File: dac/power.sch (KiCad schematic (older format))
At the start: 30 parts, among them Q2 2STD1665T4, U4 OPA830

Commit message: More work on dac/power.sch and dac/reference_buffer.sch. Also, fixed comments in input/reference_buffer.sch
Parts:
- removed C39: 1uF, Capacitor_SMD:C_0805_2012Metric, symbol Device:C_Small
- removed C7: 330uF, Capacitor_SMD:CP_Elec_8x6.7, symbol Device:CP1_Small
- removed D15: 5V (standoff), Diode_SMD:D_SMA, symbol Device:D_Zener
- removed F?: 750 mA 90 mOhm, Fuse:Fuse_1206_3216Metric, symbol Device:Polyfuse
- removed R19, R?: 180, Resistor_SMD:R_0805_2012Metric, symbol Device:R_US
- removed U4: OPA830, Package_SO:SOIC-8_3.9x4.9mm_P1.27mm, symbol ilemt_input:opamp_single
- added C11, C23, C24: 10uF, Capacitor_SMD:C_0603_1608Metric, symbol Device:C_Small
- added C21, C22: 1uF, Capacitor_SMD:C_0805_2012Metric, symbol Device:C_Small
- added C25, C26: 330uF, Capacitor_SMD:CP_Elec_8x6.7, symbol Device:CP1_Small
- added D4: 5V (standoff), Diode_SMD:D_SMA, symbol Device:D_Zener
- added FB4: 21 Ohm, Inductor_SMD:L_0805_2012Metric, symbol dk_Ferrite-Beads-and-Chips:MPZ2012S601AT000
- added J1: Aux power, digikey-footprints:PinHeader_1x3_P2.54_Drill1.1mm, symbol dk_Rectangular-Connectors-Headers-Male-Pins.lib:640456-3
- added R10, R9: 0, Resistor_SMD:R_0603_1608Metric, symbol Device:R_US
- added R12, R16, R17, R18: 200, Resistor_SMD:R_0603_1608Metric, symbol Device:R_US
- added R13, R14: 1K, Resistor_SMD:R_0603_1608Metric, symbol Device:R_US
- added TP4: +8V, TestPoint:TestPoint_THTPad_D1.5mm_Drill0.7mm, symbol Connector:TestPoint
- added TP5: -12V, TestPoint:TestPoint_THTPad_D1.5mm_Drill0.7mm, symbol Connector:TestPoint
- added U3: OP27, Package_SO:SOIC-8_3.9x4.9mm_P1.27mm, symbol ilemt_input:opamp_single
- added U5: NCP1117STAT3G, Package_TO_SOT_SMD:SOT-223, symbol dk_PMIC-Voltage-Regulators-Linear:NCP1117ST33T3G
- added U6: LM337_SOT223, Package_TO_SOT_SMD:SOT-223-3_TabPin2, symbol Regulator_Linear:LM337_SOT223
- C12: value 47pF -> 220pF
- D8: value 10V (standoff) -> 15V (standoff); DK line 41 -> (none); Description TVS DIODE 10V 17V DO214AC -> (none); Digikey 732-9947-1-ND -> (none); MPN 824500500 -> (none); Manufacturer Würth Elektronik -> (none)
- R15: value 10 -> 1.74K; footprint Resistor_SMD:R_0805_2012Metric -> Resistor_SMD:R_0603_1608Metric; DK line 9 -> (none); Description RES SMD 10 OHM 5% 1/2W 0805 -> (none); Digikey 541-10TACT-ND -> (none); MPN CRCW080510R0JNEAHP -> (none); Manufacturer Vishay Dale -> (none); Notes Thick film surge resist -> (none)
- R17: value 33 -> 10
- gave numbers to parts that had none: 2
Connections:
- net labels added: U8IN, VDD
- net labels removed: FILT_+10V, FILT_-6V, OVDD, Q2E, U4+, U4-, U4OUT, U4V+, U4V-
- wire segments 99 -> 147
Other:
- note added: "Analog supplies\nV+ : +8V (200 mA max)\nV- : -12V (100 mA max)"
- note added: "C11/R13 is a low-effort 16 Hz lowpass\nto suppress HF crud that may come in on\nthe master VREF so that it does not go\ninto VCC."
- note added: "C20 ESR is critical for stability. It acts as a subber to\nstabilize the interaction with low-ESR ceramic \nbypass caps. This is an aluminum solid polymer type, \nchosen to have ESR near 25 mOhm.\nIf the ESR is too low it will be destabilizing.\n\nD4 prevents VCC from floating up\nif current is sourced into VCC,\nor on startup."
- note added: "DAC analog supply\nVCC : +5V (80 mA max)"
- note added: "DAC digital supply\nVDD : +3.3V (100 mA max, 25 mA typ)"
- note added: "FB4 and R10 prevent open-loop\nHF parastitic instability in Q1, when\nlooking into the capacitive load. \n\nOn an output short, current limiting\nis imposed by dragging down V+,\nwhich is current limited by U5."
- note added: "R12 prevents U3 from having to source current\nnear its positive rail. Instead it is always sinking,\na nominal current of 8 mA."
- note added: "Remote sense at bus"
- note added: "These supplies are mainly for the output opamps, but the\nnoise-critical DAC analog VCC supply is drawn from V+ also."
- note added: "VCC is noise critical because the DAC reference\nis with respect to VCC. Any 1/f noise in VCC will\nshow up on the ADC reference. See reference_buffer."
- note added: "We need a more negative supply than -6V, so that will\ncome in here from somewhere else."
- note removed: "### use opamp with low 1/f noise, doesn't really need all that bandwidth\nAny 1/f noise in VCC is going to appear in the VCOM DAC reference."
- note removed: "+3.3V digital"
- note removed: "D15, D16 prevent V+/V- from floating up\nif current is sourced into the rails, such as\nfrom the sensor input via the clamp diodes."
- note removed: "Note: \nF1, F2 fuse resistance is part of loop compensation.\nIf resistance is far from 100 mOhm this affects bandwidth \nand stability. This part has a low spread between pre-trip\nand post-trip resistance Resistance was the primary selection\ncriterion. Getting a low enough resistance forces a \nsomewhat high trip current. \n\nC14, C15 ESR is critical for stability. This is an aluminum\nsolid p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"
- note removed: "R15/C7 and R16/C11 boost the 10 kHz supply rejection\nabove the U5, U6 PSRR (which will be low in a high speed type)"
- note removed: "Remote sense at bus tap"
- note removed: "These regulators for the V+, V- analog supplies operate at a lowish dropout of about 1.5V\nand clean up any crud on the incoming supplies. They also give a supply referenced\nto the local ground which is extremely stiff at our operating frequency near 10 kHz.\nThis prevents coupling between channels via the supply. \n\nThe outputs are derived from the VREF 5V reference, which has to be low noise,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"
- note removed: "VCC regulator, +5V"
- moved on the sheet: C12, C14, C15, C16, C18, C19, C20, C27, D2, D3, FB2, FB3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

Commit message: Much progress on the DAC card.  Schematic is complete, starting on placement.
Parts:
- removed C11, C23, C24: 10uF, Capacitor_SMD:C_0603_1608Metric, symbol Device:C_Small
- removed C20, C21, C25, C26: 330uF, Capacitor_SMD:CP_Elec_8x6.7, symbol Device:CP1_Small
- removed C32: 10nF, Capacitor_SMD:C_0805_2012Metric, symbol Device:C_Small
- removed D4: 10V (standoff), Diode_SMD:D_SMA, symbol Device:D_Zener
- added C15, C16, C22, C23: 47uF, Capacitor_SMD:CP_Elec_6.3x7.7, symbol Device:CP1_Small
- added C20, C21, C8: 10uF 16V, Capacitor_SMD:C_0805_2012Metric, symbol Device:C_Small
- added D2, D5, D6: 15V (standoff), Diode_SMD:D_SMA, symbol Device:D_Zener
- C14: renamed from C12; Description 47pF ±5% 50V Ceramic Capacitor C0G, NP0 0603 (1608 Metric) -> (none); Digikey 311-1065-1-ND -> (none); MPN CC0603JRNPO9BN470 -> (none); Manufacturer Yageo -> (none)
- R16: renamed from R17; footprint Resistor_SMD:R_0603_1608Metric -> Resistor_SMD:R_0805_2012Metric; Description RES 33 OHM 1% 1/10W 0603 -> RES SMD 10 OHM 5% 1/2W 0805; Digikey RMCF0603FT33R0CT-ND -> 541-10TACT-ND; MPN RMCF0603FT33R0 -> CRCW080510R0JNEAHP; Manufacturer Stackpole Electronics Inc -> Vishay Dale; Notes (none) -> Thick film surge resist
- TP2: renamed from TP6; footprint TestPoint:TestPoint_THTPad_D1.5mm_Drill0.7mm -> TestPoint:TestPoint_Keystone_5000-5004_Miniature
- TP3: renamed from TP8; value +5V VCC -> +5V DAC_VCC; footprint TestPoint:TestPoint_THTPad_D1.5mm_Drill0.7mm -> TestPoint:TestPoint_Keystone_5000-5004_Miniature
- TP4, TP5: footprint TestPoint:TestPoint_THTPad_D1.5mm_Drill0.7mm -> TestPoint:TestPoint_Keystone_5000-5004_Miniature
- U3: value OP27 -> OPA1611; DK line 15 -> (none); Description IC OPAMP GP 1 CIRCUIT 8SOIC -> (none); Digikey 296-31706-1-ND -> (none); MPN OPA27GU/2K5 -> (none); Manufacturer Texas Instruments -> (none)
- renumbered C22 to C10, C16 to C11, C17 to C12, C25 to C13, C14 to C17, C21 to C18, C22 to C19, C8 to C9, D8 to D3, FB3 to FB1, FB1 to FB3, J1 to J5, Q2 to Q1, R9 to R14, R10 to R15, R12 to R17, R14 to R19, R15 to R20, R16 to R21, R17 to R22, TP4 to TP6
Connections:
- net VDD is gone; now on net VCC: C13.1, TP2.1, U4.3 (VO)
- net GND: now also C15.2, C16.1, C20.1, C21.1, C22.2, C23.1, C8.1, D2.2 (A)
- net V+: now also C22.1, D6.2 (A)
- net V-: now also C23.2, D5.1 (K)
- net VCC: no longer C17.1, D4.1 (K), FB4.2, R18.2, TP3.1
- net U3-: now reaches C14.1, R18.1, U3.2 (-)
- net Q1E: now reaches C14.2, FB4.1, Q1.3 (E)
- net Q1B: now reaches Q1.1 (B), R16.1, R17.2
- net V-_UNREG: now reaches C12.1, C19.2, D3.2 (A), FB3.2, U6.2 (VI)
- net V-_UNREG: now also C16.2, D5.2 (A)
- net V-_RAW: now reaches FB3.1, J5.3, R15.2
- net V+_RAW: now reaches FB2.1, J5.2, R14.2
- net V+_ADJ: now reaches R19.1, R21.1, U5.1 (ADJ/GND)
- net V+_ADJ: now also C20.2
- net V-_ADJ: now reaches R20.1, R22.1, U6.1 (ADJ)
- net V-_ADJ: now also C21.2
- net U3+: now reaches R13.1, U3.3 (+)
- net U3+: now also C8.2
- net RAW_+10V renamed +10V
- net RAW_+5VDIG renamed +5VDIG
- net RAW_-6V renamed -6V
- net U7IN renamed U4_IN
- net U8IN renamed V+_UNREG
- net V+_UNREG: now also C15.1, D2.1 (K), D6.1 (K)
- new net DAC_VCC: C17.1, D4.1 (K), FB4.2, R18.2, TP3.1
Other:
- note added: "Analog supplies\nV+ : +8V (200 mA max)\nV- : -12V (200 mA max)"
- note added: "C17 ESR is critical for stability. If the ESR is too low it\nwill be destabilizing. It acts as a snubber to stabilize\nthe interaction with low-ESR ceramic bypass caps. This is\nan aluminum solid polymer type, chosen to have ESR near 25\nmOhm.\n\nD4 prevents VCC from floating up if current is sourced into\nVCC, or on startup."
- note added: "C8/R13 is a low-effort 16 Hz lowpass\nto suppress HF crud that may come in on\nthe master VREF so that it does not go\ninto DAC_VCC."
- note added: "D5, D6 are being used as ordinary diodes. As well as the\nclassic regulator protection function, these also work with\nD2, D3 to prevent the rails from rising if current is sourced\nin, such as from protection diodes."
- note added: "DAC analog supply\nDAC_VCC : +5V (80 mA max)"
- note added: "DAC_VCC is noise critical because the DAC reference\nis with respect to VCC. Any 1/f noise in VCC will\nshow up on the ADC reference. See reference_buffer."
- note added: "Digital supply\nVCC : +3.3V (100 mA max, 25 mA typ)"
- note added: "FB4 and R16 prevent open-loop\nHF parastitic instability in Q1, when\nlooking into the capacitive load. \n\nOn an output short, current limiting\nis imposed by dragging down V+,\nwhich is current limited by U5."
- note added: "R17 prevents U3 from having to source current\nnear its positive rail. Instead it is always sinking,\na nominal current of 8 mA."
- note added: "This net is forced to be called VCC because\nit connects to hidden pins on logic."
- note removed: "Analog supplies\nV+ : +8V (200 mA max)\nV- : -12V (100 mA max)"
- note removed: "C11/R13 is a low-effort 16 Hz lowpass\nto suppress HF crud that may come in on\nthe master VREF so that it does not go\ninto VCC."
- note removed: "C20 ESR is critical for stability. It acts as a subber to\nstabilize the interaction with low-ESR ceramic \nbypass caps. This is an aluminum solid polymer type, \nchosen to have ESR near 25 mOhm.\nIf the ESR is too low it will be destabilizing.\n\nD4 prevents VCC from floating up\nif current is sourced into VCC,\nor on startup."
- note removed: "DAC analog supply\nVCC : +5V (80 mA max)"
- note removed: "DAC digital supply\nVDD : +3.3V (100 mA max, 25 mA typ)"
- note removed: "FB4 and R10 prevent open-loop\nHF parastitic instability in Q1, when\nlooking into the capacitive load. \n\nOn an output short, current limiting\nis imposed by dragging down V+,\nwhich is current limited by U5."
- note removed: "R12 prevents U3 from having to source current\nnear its positive rail. Instead it is always sinking,\na nominal current of 8 mA."
- note removed: "VCC is noise critical because the DAC reference\nis with respect to VCC. Any 1/f noise in VCC will\nshow up on the ADC reference. See reference_buffer."
- moved on the sheet: C10, C11, C12, C13, C14, C17, C18, C19, C9, D1, D3, D4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

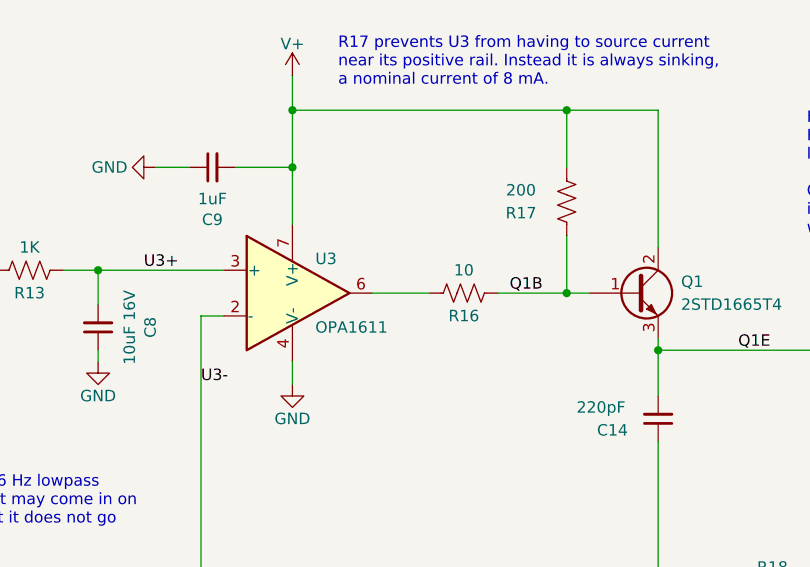
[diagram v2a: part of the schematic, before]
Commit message: DAC board is routed.  I also changed the digital interface to use a buffer (like I did on the input board) so that everything is buffered and we don't have multi-drop nets.
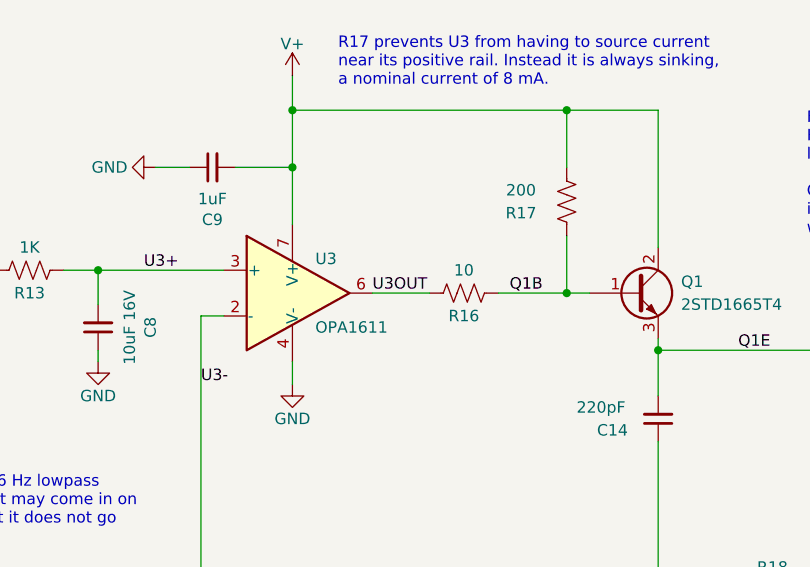
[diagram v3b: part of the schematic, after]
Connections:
- net U3OUT: now reaches R16.2, U3.6
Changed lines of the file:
@@
 Text Label 11250 5650 0    50   ~ 0
 U4_IN
+Text Label 3100 7950 0    50   ~ 0
+U3OUT
 $EndSCHEMATC
